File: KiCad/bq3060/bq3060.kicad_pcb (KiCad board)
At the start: 2 copper layers, 68 parts, among them J1 Conn_01x04_Male, J2 Conn_01x03_Male, J3 Conn_01x03_Male, Q1 Si1023x, Q2 Si1023x, Q3 NDS351AN, Q4 SI4435DYTRPBF, Q5 SI4435DYTRPBF, Q6 SI4435DYTRPBF, U1 BQ29412DCT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

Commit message: Routing attempt
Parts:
- removed C1: 0.1uF, Capacitor_SMD:C_0805_2012Metric_Pad1.15x1.40mm_HandSolder
- added J4: Conn_01x03_Male, Connector_Wire:SolderWirePad_1x03_P5.715mm_Drill2mm, F.Cu at (293.6, 85.1)
- added J5: Conn_01x02_Male, Connector_Wire:SolderWirePad_1x02_P7.62mm_Drill2mm, F.Cu at (293.6, 102.4)
- moved J1 187.5 mm to (327.9, 108.2), turned to 270 degrees
- moved J2 171.9 mm to (349.2, 84.1)
- moved J3 164.5 mm to (330.7, 62.0)
- moved Q6 163.8 mm to (334.8, 34.0)
- moved R28 155.9 mm to (329.2, 101.9)
- moved D2 154.7 mm to (329.7, 96.3), turned to 180 degrees
- moved Q4 137.2 mm to (320.0, 21.6)
- moved R29 132.7 mm to (333.3, 101.9)
- moved C21 130.9 mm to (329.2, 99.6)
- moved C22 129.7 mm to (333.2, 99.6)
- moved R31 123.7 mm to (333.3, 103.9)
- moved R27 122.1 mm to (329.2, 103.9)
- moved R22 119.6 mm to (334.8, 76.5)
- moved R20 114.0 mm to (307.3, 26.9)
- moved R30 113.6 mm to (324.1, 66.0)
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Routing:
- net Net-(C10-Pad1): track 0.00 -> 32.6 mm
- net 4P: track 0.00 -> 31.4 mm
- net 2P: track 0.00 -> 24.5 mm
- net 1P: track 0.00 -> 24.5 mm
- net 3P: track 0.00 -> 24.4 mm
- net 1N: track 0.00 -> 16.9 mm
- net TP3: track 0.00 -> 16.5 mm
- net TP4: track 0.00 -> 14.3 mm
- net Net-(C7-Pad2): track 0.00 -> 13.9 mm
- net Net-(C21-Pad1): track 0.00 -> 12.1 mm
- net Net-(R27-Pad1): track 0.00 -> 8.73 mm
- net Net-(C1-Pad1): track 0.00 -> 8.48 mm
- net Net-(R28-Pad1): track 0.00 -> 8.42 mm
- net Net-(C21-Pad2): track 0.00 -> 7.85 mm
- net Net-(C5-Pad2): track 0.00 -> 7.81 mm
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
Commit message: Tried routing again
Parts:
- added C1: 0.1uF, Capacitor_SMD:C_0805_2012Metric_Pad1.15x1.40mm_HandSolder, F.Cu at (289.6, 91.9)
- moved J5 182.2 mm to (112.4, 83.2), turned to 90 degrees
- moved J4 179.5 mm to (114.3, 92.1), turned to 0 degrees
- moved Q6 162.5 mm to (218.5, 147.6)
- moved R20 160.2 mm to (207.2, 152.0)
- moved C17 158.6 mm to (176.8, 135.5)
- moved Q4 157.2 mm to (218.5, 141.7)
- moved U2 156.5 mm to (166.4, 136.5)
- moved J2 150.6 mm to (198.7, 86.7)
- moved Q3 150.0 mm to (296.2, 79.0)
- moved Q5 144.7 mm to (218.5, 153.8), turned to 0 degrees
- moved R21 142.9 mm to (212.2, 147.5), turned to 180 degrees
- moved R22 139.7 mm to (212.2, 143.5), turned to 180 degrees
- moved R18 139.2 mm to (212.2, 145.5)
- moved D3 137.0 mm to (213.2, 152.7), turned to 90 degrees
- moved J1 133.6 mm to (198.7, 74.4), turned to 0 degrees
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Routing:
- net Net-(C18-Pad2): track 0.00 -> 36.6 mm
- net Net-(C10-Pad1): track 32.6 -> 0.00 mm
- net 2P: track 24.5 -> 0.00 mm
- net 1P: track 24.5 -> 0.00 mm
- net 3P: track 24.4 -> 0.00 mm
- net Net-(Q5-Pad4): track 0.00 -> 20.1 mm, vias 0 -> 2
- net TP3: track 16.5 -> 0.00 mm
- net 4P: track 31.4 -> 16.0 mm
- net TP4: track 14.3 -> 0.00 mm
- net Net-(C7-Pad2): track 13.9 -> 0.00 mm
- net Net-(Q5-Pad5): track 0.00 -> 13.4 mm
- net Net-(C21-Pad1): track 12.1 -> 0.00 mm
- net Net-(Q6-Pad4): track 0.00 -> 9.76 mm
- net Net-(R27-Pad1): track 8.73 -> 0.00 mm
- net Net-(C1-Pad1): track 8.48 -> 0.00 mm
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
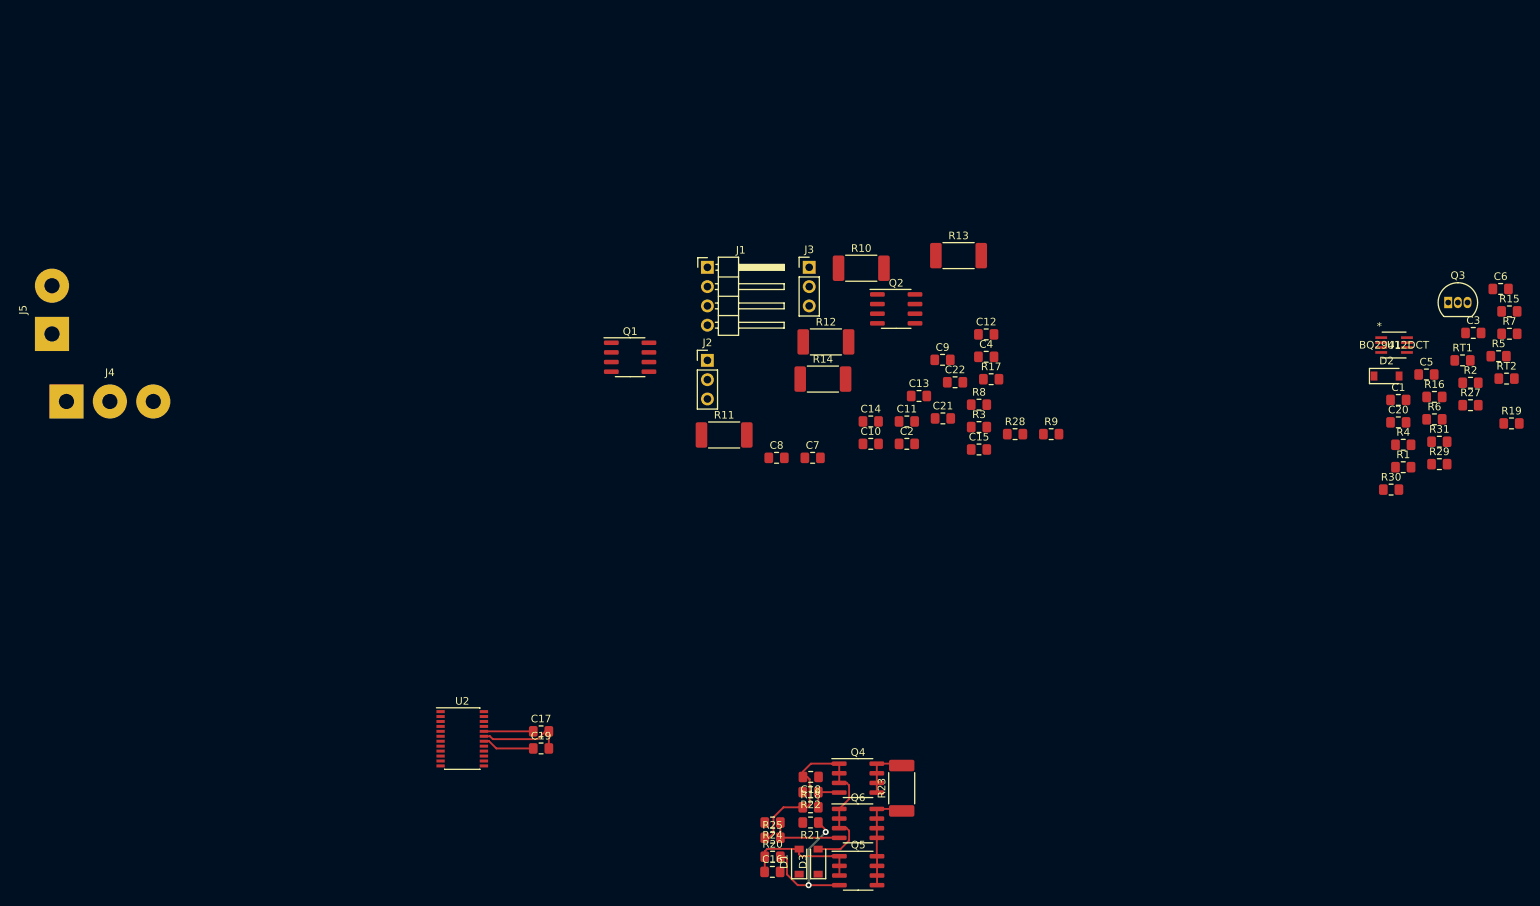
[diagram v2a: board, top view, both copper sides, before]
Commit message: Add prototype bq3060 design
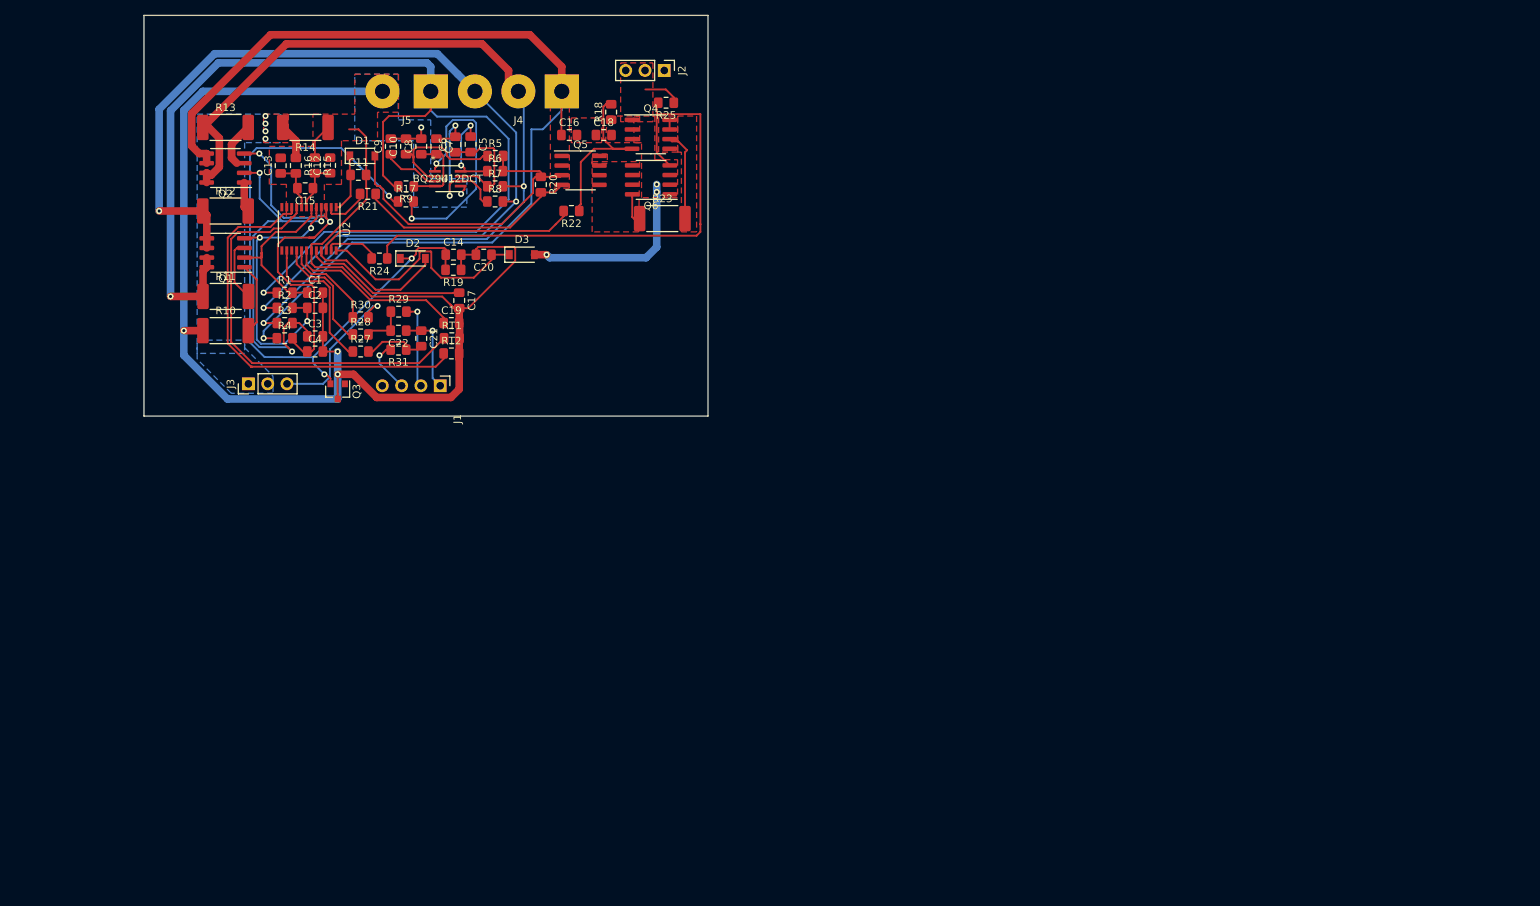
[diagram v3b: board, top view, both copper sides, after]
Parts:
- Q3: footprint Package_TO_SOT_THT:TO-92_Inline -> Package_TO_SOT_SMD:SOT-23
- moved R15 158.4 mm to (147.0, 61.0), turned to 270 degrees
- moved R2 156.4 mm to (143.0, 79.8)
- moved R16 152.9 mm to (144.5, 61.0), turned to 270 degrees
- moved C3 152.5 mm to (147.0, 83.5)
- moved R1 149.0 mm to (143.0, 77.8)
- moved R4 147.9 mm to (143.0, 83.8)
- moved Q3 146.7 mm to (150.0, 90.8), turned to 270 degrees
- moved R27 146.3 mm to (153.0, 85.5)
- moved C1 143.3 mm to (147.0, 77.8)
- moved R19 140.8 mm to (165.2, 74.8), turned to 180 degrees
- moved RT2 138.9 mm to (165.0, 85.8)
- moved C6 138.9 mm to (165.5, 58.2), turned to 90 degrees
- moved R29 138.5 mm to (158.0, 80.2)
- moved R31 137.6 mm to (158.0, 85.2), turned to 180 degrees
- moved R30 137.5 mm to (153.0, 81.0)
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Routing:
- net 1N: track 11.4 -> 211.4 mm, vias 0 -> 5
- net 4P: track 16.0 -> 176.4 mm, vias 0 -> 1
- net 1P: track 0.00 -> 155.2 mm, vias 0 -> 2
- net 2P: track 0.00 -> 130.9 mm, vias 0 -> 3
- net 3P: track 0.00 -> 120.3 mm, vias 0 -> 2
- net Net-(C14-Pad1): track 0.00 -> 89.5 mm, vias 0 -> 3
- net Net-(Q6-Pad4): track 9.76 -> 73.7 mm
- net Net-(RT2-Pad1): track 0.00 -> 56.2 mm
- net Net-(RT1-Pad1): track 0.00 -> 54.9 mm
- net Net-(C4-Pad1): track 0.00 -> 51.6 mm, vias 0 -> 2
- net Net-(C3-Pad1): track 0.00 -> 49.6 mm, vias 0 -> 3
- net Net-(C2-Pad1): track 0.00 -> 38.0 mm, vias 0 -> 3
- net Net-(R22-Pad2): track 0.00 -> 34.2 mm
- net Net-(R17-Pad2): track 0.00 -> 32.1 mm, vias 0 -> 2
- net Net-(C20-Pad1): track 0.00 -> 30.8 mm
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- added copper zone on B.Cu, net 1N
- added copper zone on F.Cu, net 1N
- added copper zone on F.Cu, net 4P
- added copper zone on F.Cu, net Net-(C16-Pad2)
- added copper zone on F.Cu, net Net-(C18-Pad2)
- added copper zone on B.Cu, net Net-(J3-Pad1)
- added copper zone on F.Cu, net Net-(J3-Pad1)
- added copper zone on F.Cu, net Net-(Q4-Pad5)
- added copper zone on F.Cu, net Net-(Q5-Pad5)
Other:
- board outline added: 74.2 x 52.8 mm
